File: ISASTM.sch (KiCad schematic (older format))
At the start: 137 parts, among them J1 Bus_ISA_8bit, J2 USB_C_Receptacle_USB2.0, J3 Boot select, J4 USB_C_Receptacle_USB2.0, J5 TagConnect_TC2030_SWD, SW1 Reset, U1 STM32H743IITx, U10 SN74AVC8T245PW, U11 SN74AVC8T245PW, U12 SN74AVC8T245PW, U13 SN74AVC8T245PW, U14 SRV05-4, U15 USB3343, U2 MT48LC16M16A2P, U3 SN74AVC8T245PW, U4 SN74AVC8T245PW, U5 AMS1117-3.3, U6 SN74AVC8T245PW, U7 SN74AVC8T245PW, U8 SN74AVC8T245PW, U9 SN74AVC8T245PW, X1 SG-7050CAN, Y1 26 MHz, Y2 8 MHz

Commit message: Route LV bus
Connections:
- net ADDRESS_DIR: now also U1.129 (PH14)
- net CONTROL2_DIR: now also U1.88 (PH11)
- net IRQ_DIR: now also U1.24 (PF6)
- net LV_A5: now also U1.55 (PC5); no longer U1.128 (PH13)
- net LV_A6: now also U1.115 (PC6); no longer U1.129 (PH14)
- net LV_A7: now also U1.116 (PC7); no longer U1.130 (PH15)
- net LV_DRQ3: now also U1.121 (PA10); no longer U1.115 (PC6)
- net LV_IRQ3: now also U1.95 (PB15); no longer U1.26 (PF8)
- net LV_IRQ4: now also U1.99 (PD11); no longer U1.25 (PF7)
- net LV_IRQ5: now also U1.100 (PD12); no longer U1.24 (PF6)
- net LV_IRQ6: now also U1.101 (PD13); no longer U1.89 (PH12)
- net SPARE1_DIR: now also U1.94 (PB14)
- net SPARE2_DIR: now also U1.25 (PF7)
- net ~ADDRESS_OE: now also U1.130 (PH15)
- net ~CONTROL2_OE: now also U1.89 (PH12)
- net ~IRQ_OE: now also U1.128 (PH13)
- net ~SPARE1_OE: now also U1.85 (PH8)
- net ~SPARE2_OE: now also U1.26 (PF8)
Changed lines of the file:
@@
 Wire Wire Line
 	1650 4000 2050 4000
-Text Label 1700 6100 0    50   ~ 0
+Text Label 5200 5300 2    50   ~ 0
 LV_A7
-Text Label 1700 6000 0    50   ~ 0
+Text Label 5200 5200 2    50   ~ 0
 LV_A6
-Text Label 1700 5900 0    50   ~ 0
+Text Label 5200 5100 2    50   ~ 0
 LV_A5
 Wire Wire Line
@@
 	1700 5300 2050 5300
 Wire Wire Line
-	1700 5900 2050 5900
-Wire Wire Line
-	1700 6000 2050 6000
-Wire Wire Line
-	1700 6100 2050 6100
+	5200 5100 4850 5100
+Wire Wire Line
+	5200 5200 4850 5200
+Wire Wire Line
+	5200 5300 4850 5300
 Text Label 5150 6100 2    50   ~ 0
 LV_A15
@@
 Text Label 1600 6600 0    50   ~ 0
 LV_DRQ2
-Text Label 5300 5200 2    50   ~ 0
+Text Label 5300 2200 2    50   ~ 0
 LV_DRQ3
 Wire Wire Line
@@
 	1600 6600 2050 6600
 Wire Wire Line
-	4850 5200 5300 5200
+	4850 2200 5300 2200
 Text Label 5300 2000 2    50   ~ 0
 LV_DRQ1
@@
 Text Label 5450 2100 2    50   ~ 0
 LV_IRQ2
-Text Label 1450 8700 0    50   ~ 0
+Text Label 5450 7400 2    50   ~ 0
 LV_IRQ4
-Text Label 1450 8600 0    50   ~ 0
+Text Label 5450 7500 2    50   ~ 0
 LV_IRQ5
-Text Label 1450 5800 0    50   ~ 0
-LV_IRQ6
 Text Label 5450 7000 2    50   ~ 0
 LV_IRQ7
@@
 	5450 2100 4850 2100
 Wire Wire Line
-	1450 8700 2050 8700
-Wire Wire Line
-	1450 8600 2050 8600
-Wire Wire Line
-	1450 5800 2050 5800
+	5450 7400 4850 7400
+Wire Wire Line
+	5450 7500 4850 7500
 Wire Wire Line
 	5450 7000 4850 7000
@@
 Wire Wire Line
 	5400 2700 4850 2700
-Text Label 1450 8800 0    50   ~ 0
+Text Label 5450 4400 2    50   ~ 0
 LV_IRQ3
 Wire Wire Line
-	1450 8800 2050 8800
+	5450 4400 4850 4400
 Wire Wire Line
 	4850 6600 5400 6600
@@
 Wire Wire Line
 	2050 8900 1450 8900
+Text Label 5450 7600 2    50   ~ 0
+LV_IRQ6
+Wire Wire Line
+	5450 7600 4850 7600
+Wire Wire Line
+	2050 8800 1450 8800
+Text Label 1450 8800 0    50   ~ 0
+~SPARE2_OE
+Wire Wire Line
+	2050 8700 1450 8700
+Text Label 1450 8700 0    50   ~ 0
+SPARE2_DIR
+Text Label 1550 6100 0    50   ~ 0
+~ADDRESS_OE
+Wire Wire Line
+	1550 6100 2050 6100
+Wire Wire Line
+	2050 6000 1550 6000
+Text Label 1550 6000 0    50   ~ 0
+ADDRESS_DIR
+Wire Wire Line
+	2050 5900 1550 5900
+Text Label 1550 5900 0    50   ~ 0
+~IRQ_OE
+Wire Wire Line
+	2050 8600 1450 8600
+Text Label 1450 8600 0    50   ~ 0
+IRQ_DIR
+Wire Wire Line
+	4850 4300 5500 4300
+Text Label 5500 4300 2    50   ~ 0
+SPARE1_DIR
+Text Label 1450 5800 0    50   ~ 0
+~CONTROL2_OE
+Wire Wire Line
+	1450 5800 2050 5800
+Wire Wire Line
+	2050 5700 1450 5700
+Text Label 1450 5700 0    50   ~ 0
+CONTROL2_DIR
+Wire Wire Line
+	2050 5400 1450 5400
+Text Label 1450 5400 0    50   ~ 0
+~SPARE1_OE
 $EndSCHEMATC

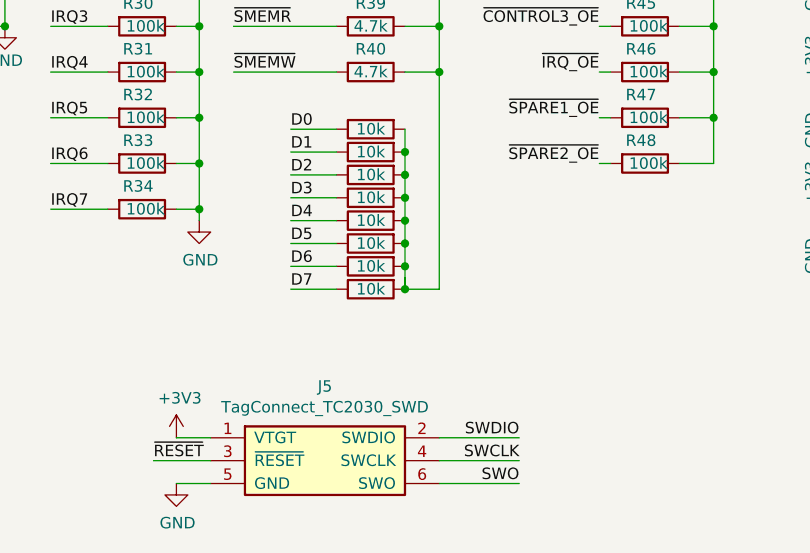
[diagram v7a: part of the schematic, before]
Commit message: Place bias resistors
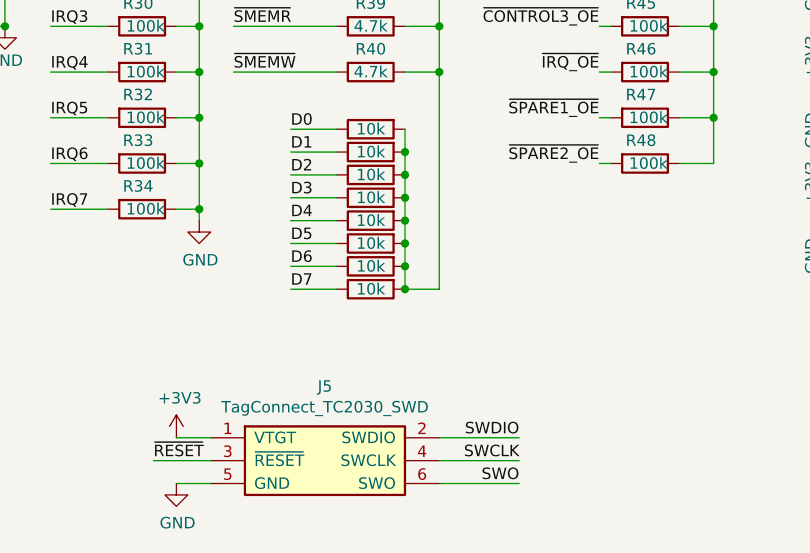
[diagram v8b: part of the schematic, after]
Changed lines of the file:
@@
 Connection ~ 16850 13300
-Wire Wire Line
-	17750 14600 17750 14650
 Wire Wire Line
 	17750 14550 17750 14650
